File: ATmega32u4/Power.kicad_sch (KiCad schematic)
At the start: 8 parts, among them U1 AMS1117-3.3

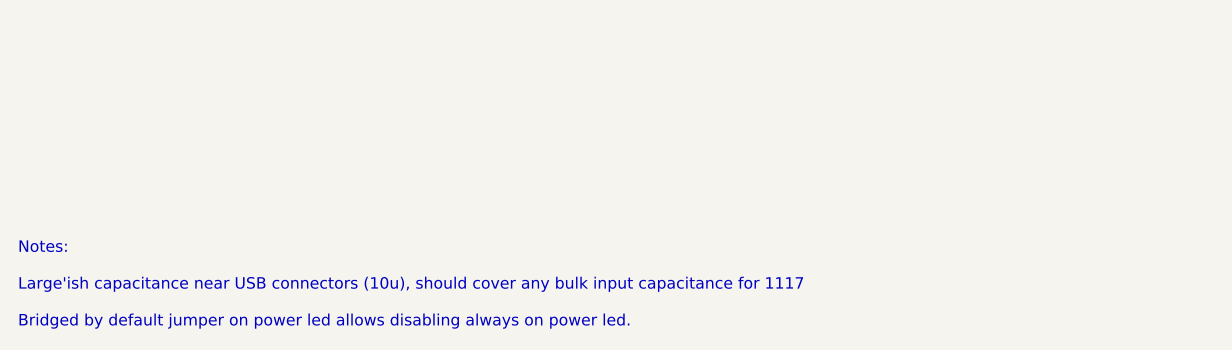
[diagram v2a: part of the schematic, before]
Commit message: Update notes, add io for reading cc pins, minor changes to schematic and routing.
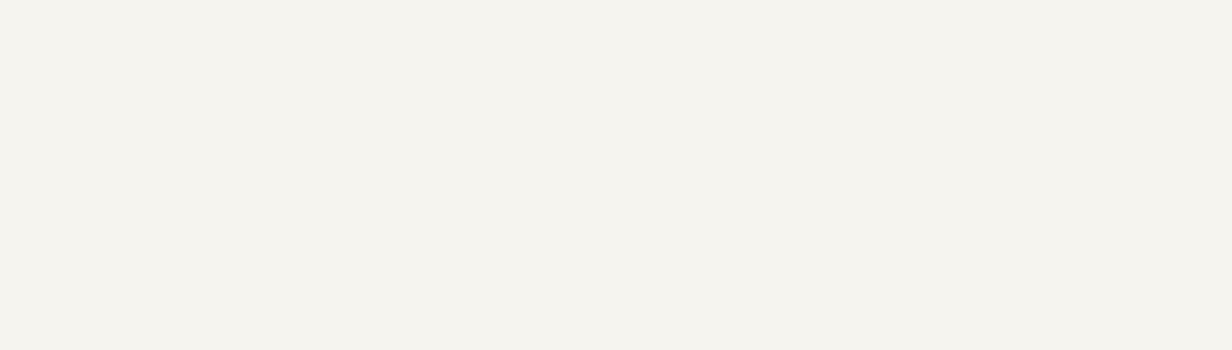
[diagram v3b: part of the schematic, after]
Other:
- note removed: "Notes: Large'ish capacitance near USB connectors (10u), should cover any bulk input capacitance for 1117 Bridged by default jumper on power led allows disabling always on power led."
- title: (none) -> OpenRetroPad
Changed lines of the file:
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@@
 (kicad_sch (version 20211123) (generator eeschema)
   (paper "A4")
+  (title_block
+    (title "OpenRetroPad")
+    (date "2022-12-29")
+    (rev "2")
+    (comment 3 "github.com/OpenRetroPad")
+    (comment 4 "ATmega32u4")
+  )
   (junction (at 172.72 92.71) (diameter 0) (color 0 0 0 0)
   )
@@
     (effects (font (size 1.27 1.27)) (justify left bottom))
   )
-  (text "Notes:\n\nLarge'ish capacitance near USB connectors (10u), should cover any bulk input capacitance for 1117\n\nBridged by default jumper on power led allows disabling always on power led."
-    (at 12.7 196.85 0)
-    (effects (font (size 1.27 1.27)) (justify left bottom))
-  )
